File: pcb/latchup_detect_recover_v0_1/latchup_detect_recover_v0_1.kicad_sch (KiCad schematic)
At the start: 4 parts, among them Q1 IPD380P06NMATMA1, U1 SN74HC14ADBR

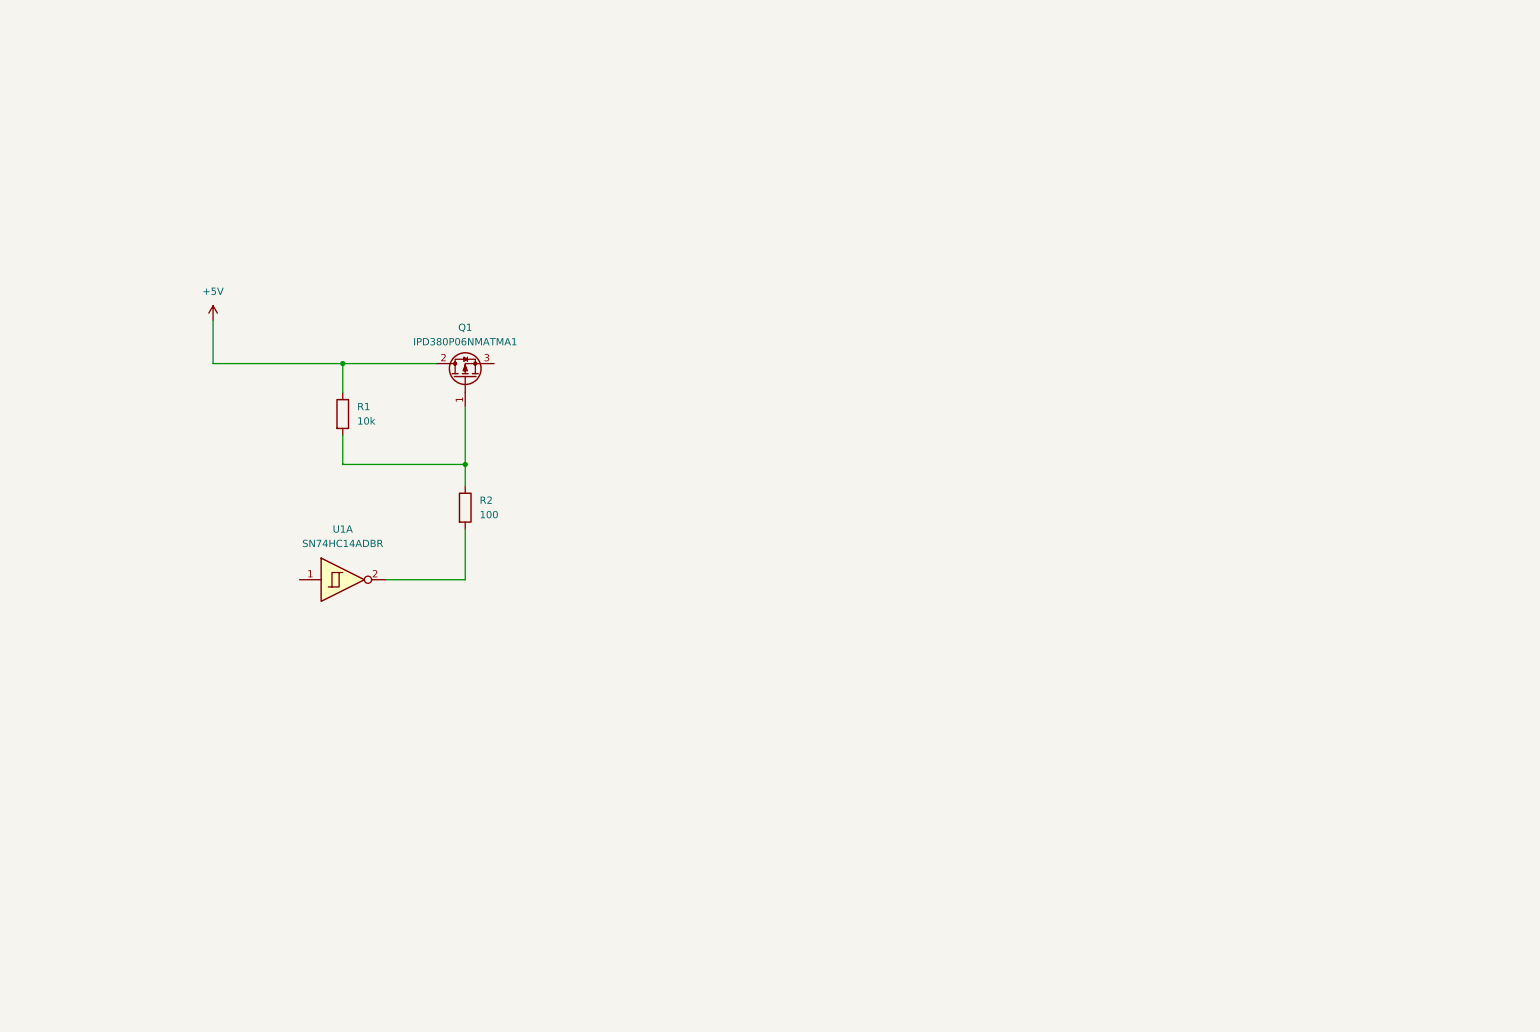
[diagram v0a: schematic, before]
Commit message: schematic has amp and comp
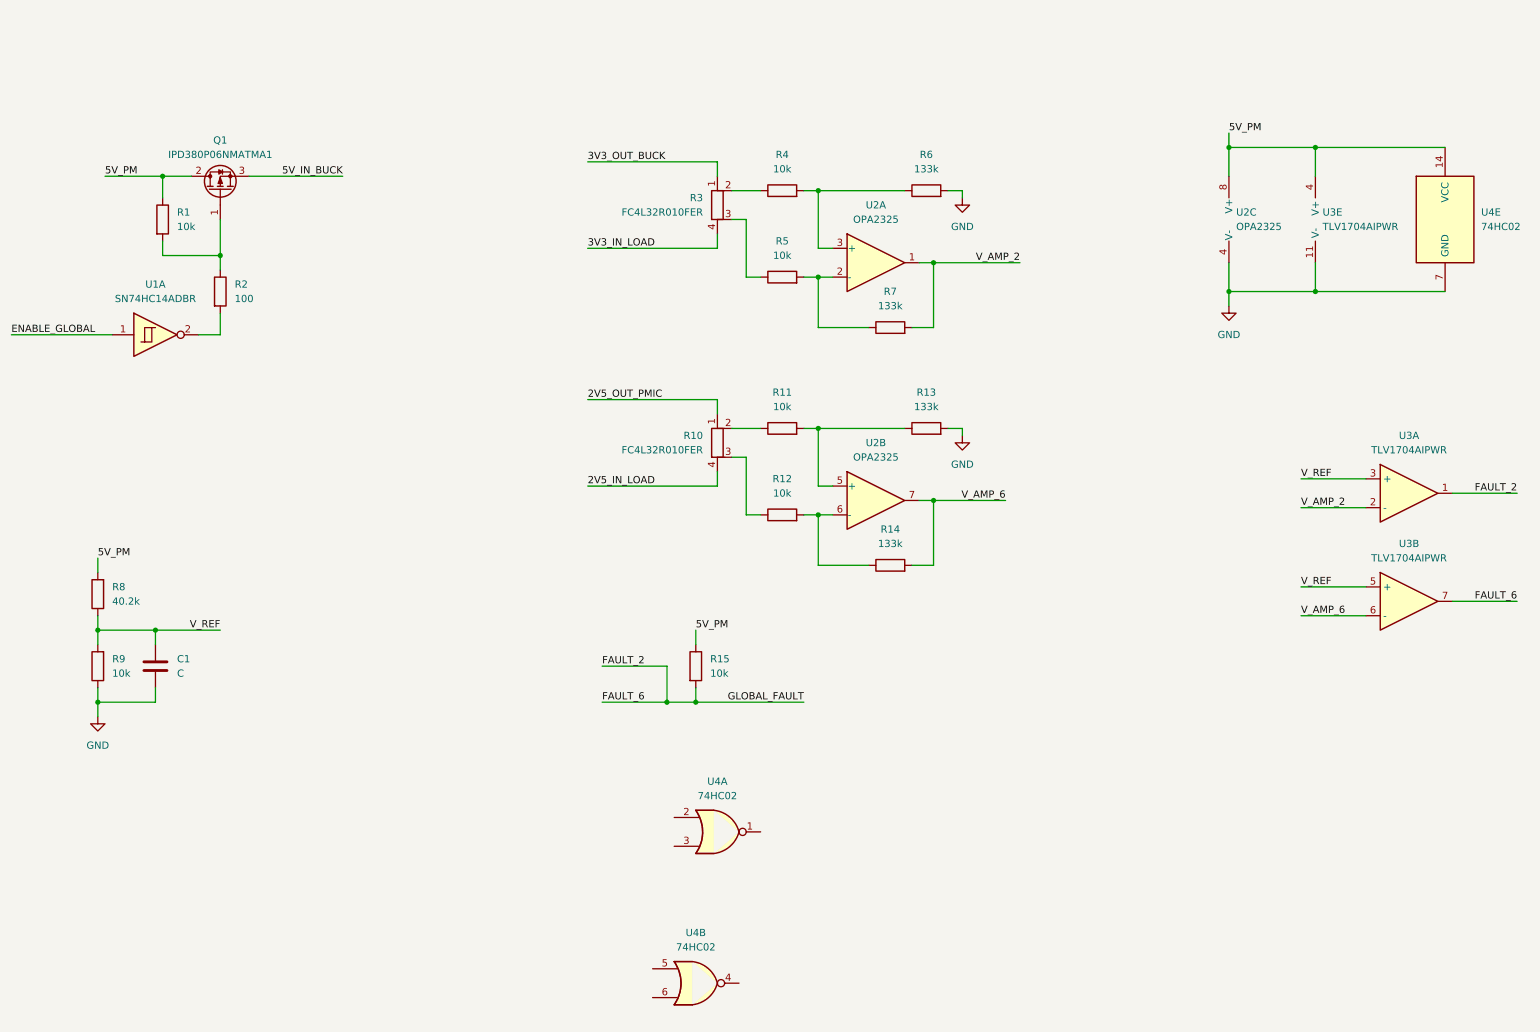
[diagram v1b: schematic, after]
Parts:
- added C1: C, Capacitor_SMD:C_0805_2012Metric_Pad1.18x1.45mm_HandSolder, symbol Device:C
- added R10, R3: FC4L32R010FER, symbol Device:R_Shunt
- added R11, R12, R15, R4, R5, R9: 10k, Resistor_SMD:R_0805_2012Metric, symbol Device:R
- added R13, R14, R6, R7: 133k, Resistor_SMD:R_0805_2012Metric, symbol Device:R
- added R8: 40.2k, Resistor_SMD:R_0805_2012Metric, symbol Device:R
- added U2: OPA2325, Package_SO:SOIC-8_3.9x4.9mm_P1.27mm, symbol Amplifier_Operational:OPA2325
- added U3: TLV1704AIPWR, Package_SO:TSSOP-14_4.4x5mm_P0.65mm, symbol Device:Opamp_Quad
- added U4: 74HC02, Package_SO:SOIC-14-16_3.9x9.9mm_P1.27mm, symbol 74xx:74HC02
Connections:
- net 5V_IN_BUCK: now reaches Q1.3 (S)
- net ENABLE_GLOBAL: now reaches U1.1
- net +5V renamed 5V_PM
- net 5V_PM: now also R15.1, R8.2, U2.8 (V+), U3.4 (V+), U4.14 (VCC)
- new net: R3.3, R5.1
- new net: R5.2, R7.1, U2.2 (-)
- new net: R10.2, R11.1
- new net: R11.2, R13.1, U2.5 (+)
- new net: R12.2, R14.1, U2.6 (-)
- new net: R3.2, R4.1
- new net: R4.2, R6.1, U2.3 (+)
- new net: R10.3, R12.1
- new net 2V5_IN_LOAD: R10.4
- new net 2V5_OUT_PMIC: R10.1
- new net 3V3_IN_LOAD: R3.4
- new net 3V3_OUT_BUCK: R3.1
- new net FAULT_2: R15.2, U3.1, U3.7
- new net GND: C1.2, R13.2, R6.2, R9.1, U2.4 (V-), U3.11 (V-), U4.7 (GND)
- new net V_AMP_2: R7.2, U2.1, U3.2 (-)
- new net V_AMP_6: R14.2, U2.7, U3.6 (-)
- new net V_REF: C1.1, R8.1, R9.2, U3.3 (+), U3.5 (+)
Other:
- moved on the sheet: Q1, R1, R2, U1A

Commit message: import lib for or gate and shunt
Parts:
- removed R3: FC4L32R010FER, symbol Device:R_Shunt
- removed U4: 74HC02, Package_SO:SOIC-14-16_3.9x9.9mm_P1.27mm, symbol 74xx:74HC02
- added U4: SN74HC32PWR, SN74HC32PWR:SOP65P640X120-14N, symbol SN74HC32PWR:SN74HC32PWR
- added U5, U6: FC4L32R050FER, FC4L32_OHM, symbol FC4L32R050FER:FC4L32R050FER
- C1: value C -> 100nF
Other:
- moved on the sheet: U3A, U3B
